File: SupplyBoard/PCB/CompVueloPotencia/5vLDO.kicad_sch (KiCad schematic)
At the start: 7 parts, among them U12 LD39200DPUR

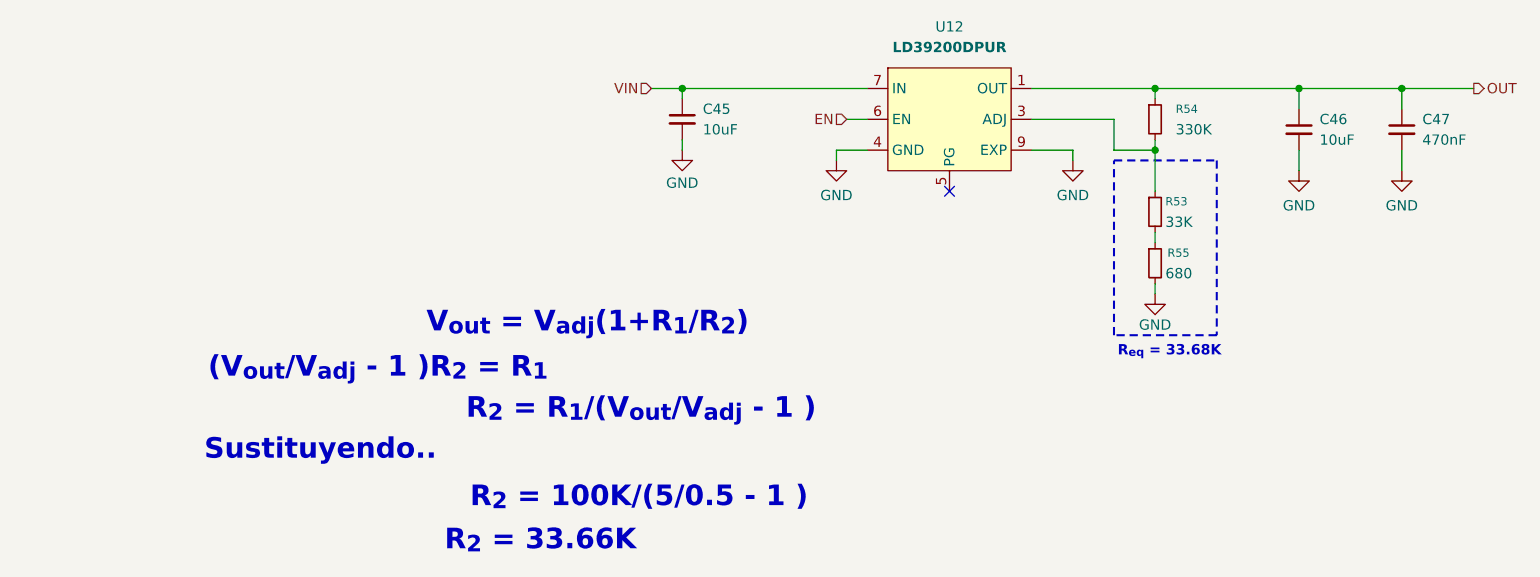
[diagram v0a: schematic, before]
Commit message: SupplyBoard - update layout
schematic completed and PCB layout started; only the routing of the traces remains to be done
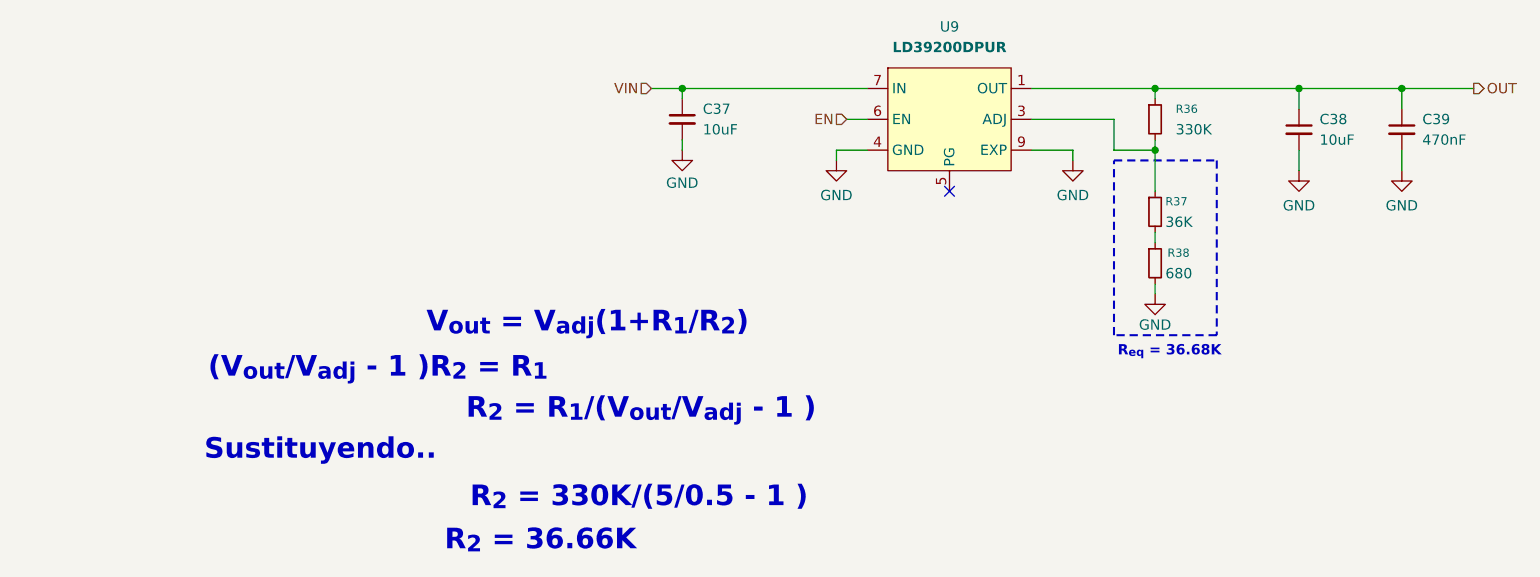
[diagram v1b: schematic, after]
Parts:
- C37: renamed from C45; footprint (none) -> Capacitor_SMD:C_0805_2012Metric_Pad1.18x1.45mm_HandSolder
- C38: renamed from C46; footprint (none) -> Capacitor_SMD:C_0805_2012Metric_Pad1.18x1.45mm_HandSolder
- C39: renamed from C47; footprint (none) -> Capacitor_SMD:C_0805_2012Metric_Pad1.18x1.45mm_HandSolder
- R36: renamed from R54; footprint (none) -> Resistor_SMD:R_0805_2012Metric_Pad1.20x1.40mm_HandSolder
- R37: renamed from R53; value 33K -> 36K; footprint (none) -> Resistor_SMD:R_0805_2012Metric_Pad1.20x1.40mm_HandSolder
- R38: renamed from R55; footprint (none) -> Resistor_SMD:R_0805_2012Metric_Pad1.20x1.40mm_HandSolder
- renumbered U12 to U9
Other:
- note added: "R_{2} = 330K/(5/0.5 - 1 )"
- note added: "R_{2} = 36.66K"
- note added: "R_{eq} = 36.68K"
- note removed: "R_{2} = 100K/(5/0.5 - 1 )"
- note removed: "R_{2} = 33.66K"
- note removed: "R_{eq} = 33.68K"
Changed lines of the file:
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@@
 		)
 	)
-	(text "R_{2} = 100K/(5/0.5 - 1 )"
+	(text "R_{2} = 330K/(5/0.5 - 1 )"
 		(exclude_from_sim no)
 		(at 77.216 88.646 0)
@@
 		)
 	)
-	(text "R_{2} = 33.66K"
+	(text "R_{2} = 36.66K"
 		(exclude_from_sim no)
 		(at 65.024 93.98 0)
@@
 		)
 	)
-	(text "R_{eq} = 33.68K"
+	(text "R_{eq} = 36.68K"
 		(exclude_from_sim no)
 		(at 142.748 70.612 0)
@@
 		(on_board yes)
 		(dnp no)
-		(property "Reference" "#PWR098"
+		(property "Reference" "#PWR089"
 			(at 140.97 69.85 0)
 			(effects
@@
 			(project "SupplyBoardCompVuelo"
 				(path "/2119c5ce-afa8-4b00-8fd4-fc653d4beb45/22ae39d6-ba46-47bf-81b8-3d66f18a6610/efcc7e4b-243b-4527-8c15-6d23e19f631a/a64c0031-4716-45b1-8c69-e5f49448e67d"
-					(reference "#PWR098")
+					(reference "#PWR089")
 					(unit 1)
 				)
@@
 		(dnp no)
 		(fields_autoplaced yes)
-		(property "Reference" "C46"
+		(property "Reference" "C38"
 			(at 161.29 41.9162 0)
 			(effects
@@
 			)
 		)
-		(property "Footprint" ""
+		(property "Footprint" "Capacitor_SMD:C_0805_2012Metric_Pad1.18x1.45mm_HandSolder"
 			(at 158.75 43.18 0)
 			(effects
@@
 			(project "SupplyBoardCompVuelo"
 				(path "/2119c5ce-afa8-4b00-8fd4-fc653d4beb45/22ae39d6-ba46-47bf-81b8-3d66f18a6610/efcc7e4b-243b-4527-8c15-6d23e19f631a/a64c0031-4716-45b1-8c69-e5f49448e67d"
-					(reference "C46")
+					(reference "C38")
 					(unit 1)
 				)
@@
 		(on_board yes)
 		(dnp no)
-		(property "Reference" "R53"
+		(property "Reference" "R37"
 			(at 142.24 52.07 0)
 			(effects
@@
 			)
 		)
-		(property "Value" "33K"
+		(property "Value" "36K"
 			(at 142.24 54.61 0)
 			(effects
@@
 			)
 		)
-		(property "Footprint" ""
+		(property "Footprint" "Resistor_SMD:R_0805_2012Metric_Pad1.20x1.40mm_HandSolder"
 			(at 140.97 53.34 0)
 			(effects
@@
 			(project "SupplyBoardCompVuelo"
 				(path "/2119c5ce-afa8-4b00-8fd4-fc653d4beb45/22ae39d6-ba46-47bf-81b8-3d66f18a6610/efcc7e4b-243b-4527-8c15-6d23e19f631a/a64c0031-4716-45b1-8c69-e5f49448e67d"
-					(reference "R53")
+					(reference "R37")
 					(unit 1)
 				)
@@
 		(on_board yes)
 		(dnp no)
-		(property "Reference" "R55"
+		(property "Reference" "R38"
 			(at 142.494 58.42 0)
 			(effects
@@
 			)
 		)
-		(property "Footprint" ""
+		(property "Footprint" "Resistor_SMD:R_0805_2012Metric_Pad1.20x1.40mm_HandSolder"
 			(at 140.97 59.69 0)
 			(effects
@@
 			(project "SupplyBoardCompVuelo"
 				(path "/2119c5ce-afa8-4b00-8fd4-fc653d4beb45/22ae39d6-ba46-47bf-81b8-3d66f18a6610/efcc7e4b-243b-4527-8c15-6d23e19f631a/a64c0031-4716-45b1-8c69-e5f49448e67d"
-					(reference "R55")
+					(reference "R38")
 					(unit 1)
 				)
@@
 		(on_board yes)
 		(dnp no)
-		(property "Reference" "#PWR099"
+		(property "Reference" "#PWR090"
 			(at 158.75 54.61 0)
 			(effects
@@
 			(project "SupplyBoardCompVuelo"
 				(path "/2119c5ce-afa8-4b00-8fd4-fc653d4beb45/22ae39d6-ba46-47bf-81b8-3d66f18a6610/efcc7e4b-243b-4527-8c15-6d23e19f631a/a64c0031-4716-45b1-8c69-e5f49448e67d"
-					(reference "#PWR099")
+					(reference "#PWR090")
 					(unit 1)
 				)
@@
 		(dnp no)
 		(fields_autoplaced yes)
-		(property "Reference" "C47"
+		(property "Reference" "C39"
 			(at 173.99 41.9162 0)
 			(effects
@@
 			)
 		)
-		(property "Footprint" ""
+		(property "Footprint" "Capacitor_SMD:C_0805_2012Metric_Pad1.18x1.45mm_HandSolder"
 			(at 171.45 43.18 0)
 			(effects
@@
 			(project "SupplyBoardCompVuelo"
 				(path "/2119c5ce-afa8-4b00-8fd4-fc653d4beb45/22ae39d6-ba46-47bf-81b8-3d66f18a6610/efcc7e4b-243b-4527-8c15-6d23e19f631a/a64c0031-4716-45b1-8c69-e5f49448e67d"
-					(reference "C47")
+					(reference "C39")
 					(unit 1)
 				)
@@
 		(dnp no)
 		(fields_autoplaced yes)
-		(property "Reference" "U12"
+		(property "Reference" "U9"
 			(at 115.57 30.48 0)
 			(effects
@@
 			(project "SupplyBoardCompVuelo"
 				(path "/2119c5ce-afa8-4b00-8fd4-fc653d4beb45/22ae39d6-ba46-47bf-81b8-3d66f18a6610/efcc7e4b-243b-4527-8c15-6d23e19f631a/a64c0031-4716-45b1-8c69-e5f49448e67d"
-					(reference "U12")
+					(reference "U9")
 					(unit 1)
 				)
@@
 		(on_board yes)
 		(dnp no)
-		(property "Reference" "#PWR097"
+		(property "Reference" "#PWR088"
 			(at 130.81 53.34 0)
 			(effects
@@
 			(project "SupplyBoardCompVuelo"
 				(path "/2119c5ce-afa8-4b00-8fd4-fc653d4beb45/22ae39d6-ba46-47bf-81b8-3d66f18a6610/efcc7e4b-243b-4527-8c15-6d23e19f631a/a64c0031-4716-45b1-8c69-e5f49448e67d"
-					(reference "#PWR097")
+					(reference "#PWR088")
 					(unit 1)
 				)
@@
 		(on_board yes)
 		(dnp no)
-		(property "Reference" "#PWR095"
+		(property "Reference" "#PWR086"
 			(at 82.55 52.07 0)
 			(effects
@@
 			(project "SupplyBoardCompVuelo"
 				(path "/2119c5ce-afa8-4b00-8fd4-fc653d4beb45/22ae39d6-ba46-47bf-81b8-3d66f18a6610/efcc7e4b-243b-4527-8c15-6d23e19f631a/a64c0031-4716-45b1-8c69-e5f49448e67d"
-					(reference "#PWR095")
+					(reference "#PWR086")
 					(unit 1)
 				)
@@
 		(dnp no)
 		(fields_autoplaced yes)
-		(property "Reference" "C45"
+		(property "Reference" "C37"
 			(at 85.09 40.6462 0)
 			(effects
@@
 			)
 		)
-		(property "Footprint" ""
+		(property "Footprint" "Capacitor_SMD:C_0805_2012Metric_Pad1.18x1.45mm_HandSolder"
 			(at 82.55 41.91 0)
 			(effects
@@
 			(project "SupplyBoardCompVuelo"
 				(path "/2119c5ce-afa8-4b00-8fd4-fc653d4beb45/22ae39d6-ba46-47bf-81b8-3d66f18a6610/efcc7e4b-243b-4527-8c15-6d23e19f631a/a64c0031-4716-45b1-8c69-e5f49448e67d"
-					(reference "C45")
+					(reference "C37")
 					(unit 1)
 				)
@@
 		(on_board yes)
 		(dnp no)
-		(property "Reference" "#PWR096"
+		(property "Reference" "#PWR087"
 			(at 101.6 53.34 0)
 			(effects
@@
 			(project "SupplyBoardCompVuelo"
 				(path "/2119c5ce-afa8-4b00-8fd4-fc653d4beb45/22ae39d6-ba46-47bf-81b8-3d66f18a6610/efcc7e4b-243b-4527-8c15-6d23e19f631a/a64c0031-4716-45b1-8c69-e5f49448e67d"
-					(reference "#PWR096")
+					(reference "#PWR087")
 					(unit 1)
 				)
@@
 		(on_board yes)
 		(dnp no)
-		(property "Reference" "#PWR0100"
+		(property "Reference" "#PWR091"
 			(at 171.45 54.61 0)
 			(effects
@@
 			(project "SupplyBoardCompVuelo"
 				(path "/2119c5ce-afa8-4b00-8fd4-fc653d4beb45/22ae39d6-ba46-47bf-81b8-3d66f18a6610/efcc7e4b-243b-4527-8c15-6d23e19f631a/a64c0031-4716-45b1-8c69-e5f49448e67d"
-					(reference "#PWR0100")
+					(reference "#PWR091")
 					(unit 1)
 				)
@@
 		(dnp no)
 		(fields_autoplaced yes)
-		(property "Reference" "R54"
+		(property "Reference" "R36"
 			(at 143.51 40.6399 0)
 			(effects
@@
 			)
 		)
-		(property "Footprint" ""
+		(property "Footprint" "Resistor_SMD:R_0805_2012Metric_Pad1.20x1.40mm_HandSolder"
 			(at 140.97 41.91 0)
 			(effects
@@
 			(project "SupplyBoardCompVuelo"
 				(path "/2119c5ce-afa8-4b00-8fd4-fc653d4beb45/22ae39d6-ba46-47bf-81b8-3d66f18a6610/efcc7e4b-243b-4527-8c15-6d23e19f631a/a64c0031-4716-45b1-8c69-e5f49448e67d"
-					(reference "R54")
+					(reference "R36")
 					(unit 1)
 				)
